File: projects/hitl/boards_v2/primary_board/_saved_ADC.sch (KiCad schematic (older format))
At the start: 21 parts, among them J21 CONN_01X03, J22 CONN_01X03, J23 CONN_01X03, J24 CONN_01X03, U6 LTC2489CDEPBF

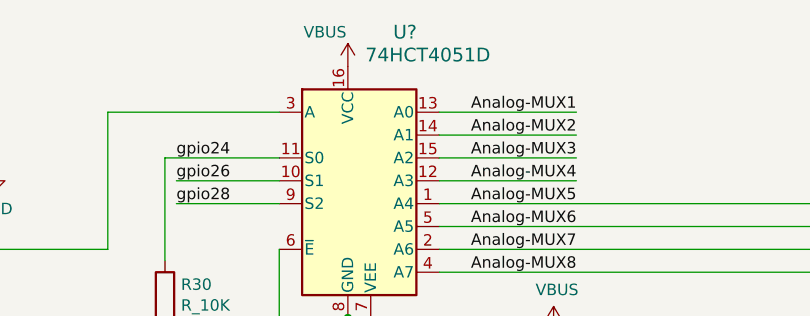
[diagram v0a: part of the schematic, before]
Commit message: Swapped out out of stock analog mux. First pass at floor planning
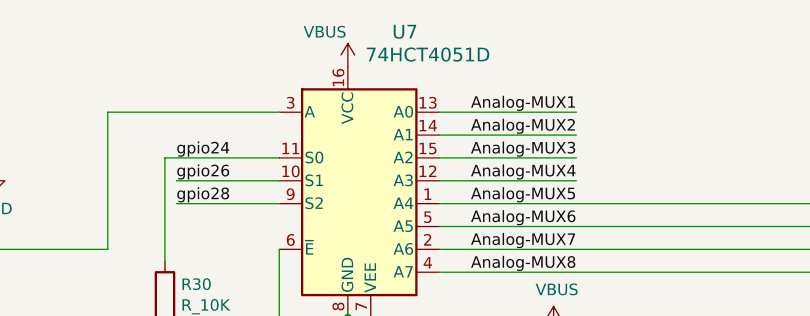
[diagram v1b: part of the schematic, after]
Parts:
- gave numbers to parts that had none: 1
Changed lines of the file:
@@
 For input voltages higher than Vbus
 $Comp
-L formula:74HCT4051D U?
+L formula:74HCT4051D U7
 U 1 1 62116DF9
 P 7050 1650
-F 0 "U?" H 7500 1900 60  0000 C CNN
+F 0 "U7" H 7500 1900 60  0000 C CNN
 F 1 "74HCT4051D" H 7600 1800 60  0000 C CNN
 F 2 "footprints:74HCT4051D" H 7850 1890 60  0001 C CNN
